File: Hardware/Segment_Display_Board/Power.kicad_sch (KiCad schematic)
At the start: 5 parts, among them J401 19V Input, U401 LM1117-5.0

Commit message: Fix stuff i guess goodnight"
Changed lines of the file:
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@@
     (title "Days Without Incident Sign")
     (date "2022-06-24")
-    (rev "v0.1-RC1")
+    (rev "${REVISION}")
     (company "FRC 1721")
+    (comment 4 "Release: ${FULL_REVISION}")
   )
   (junction (at 160.02 88.9) (diameter 0) (color 0 0 0 0)
@@
   )
   (junction (at 158.75 88.9) (diameter 0) (color 0 0 0 0)
+  )
+  (junction (at 134.62 88.9) (diameter 0) (color 0 0 0 0)
   )
   (wire (pts (xy 137.16 93.98) (xy 133.35 93.98))
@@
     (stroke (width 0) (type default) (color 0 0 0 0))
   )
-  (wire (pts (xy 133.35 88.9) (xy 137.16 88.9))
+  (wire (pts (xy 133.35 88.9) (xy 134.62 88.9))
     (stroke (width 0) (type default) (color 0 0 0 0))
   )
@@
   )
   (wire (pts (xy 167.64 88.9) (xy 170.18 88.9))
+    (stroke (width 0) (type default) (color 0 0 0 0))
+  )
+  (wire (pts (xy 134.62 88.9) (xy 137.16 88.9))
     (stroke (width 0) (type default) (color 0 0 0 0))
   )
@@
       (effects (font (size 1.27 1.27)) hide)
     )
+    (pin "1")
+  )
+  (symbol (lib_id "power:PWR_FLAG") (at 134.62 88.9 0) (unit 1)
+    (in_bom yes) (on_board yes) (fields_autoplaced)
+    (property "Reference" "#FLG0401" (id 0) (at 134.62 86.995 0)
+      (effects (font (size 1.27 1.27)) hide)
+    )
+    (property "Value" "PWR_FLAG" (id 1) (at 134.62 83.185 0)
+      (effects (font (size 1.27 1.27)) hide)
+    )
+    (property "Footprint" "" (id 2) (at 134.62 88.9 0)
+      (effects (font (size 1.27 1.27)) hide)
+    )
+    (property "Datasheet" "~" (id 3) (at 134.62 88.9 0)
+      (effects (font (size 1.27 1.27)) hide)
+    )

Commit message: Use a different regulator
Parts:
- U401: value LM1117-5.0 -> NCV1117ST50T3G
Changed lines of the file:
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@@
     (in_bom yes) (on_board yes)
     (property "Reference" "U401" (id 0) (at 151.13 95.25 0))
-    (property "Value" "LM1117-5.0" (id 1) (at 148.59 85.09 0))
+    (property "Value" "NCV1117ST50T3G" (id 1) (at 148.59 85.09 0))
     (property "Footprint" "Package_TO_SOT_SMD:SOT-223" (id 2) (at 148.59 88.9 0)
       (effects (font (size 1.27 1.27)) hide)

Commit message: include fixups fro EE
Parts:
- added C401: 10uf, Capacitor_SMD:CP_Elec_4x3, symbol Device:C_Polarized_Small
- added C402: 100nF, Capacitor_SMD:C_0805_2012Metric, symbol Device:C_Small
- added C404: 1uf, Capacitor_SMD:CP_Elec_4x3, symbol Device:C_Polarized_Small
- renumbered C401 to C403
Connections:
- net +19V: now also C401.1, C402.1
- net +5V: now also C404.1
- net GND: now also C401.2, C402.2, C404.2
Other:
- note removed: "I dont think this regulator can take this voltage, ask Mark."
- moved on the sheet: D401, J401, R401

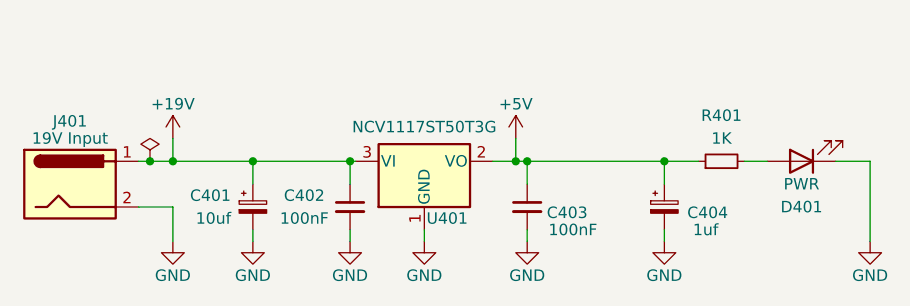
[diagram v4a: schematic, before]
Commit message: Change package for 1uF capacitor
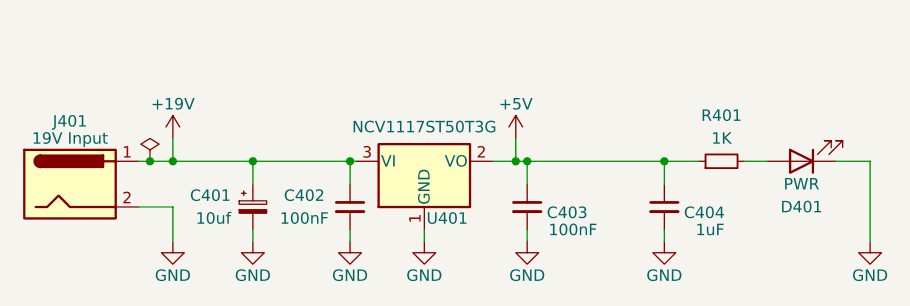
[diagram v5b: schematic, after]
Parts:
- removed C404: 1uf, Capacitor_SMD:CP_Elec_4x3, symbol Device:C_Polarized_Small
- added C404: 1uF, Capacitor_SMD:C_0805_2012Metric, symbol Device:C_Small
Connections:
- net +5V: now also C404.1
- net GND: now also C404.2
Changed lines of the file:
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@@
     (pin "1")
+  )
+  (symbol (lib_id "Device:C_Small") (at 175.26 93.98 0) (unit 1)
+    (in_bom yes) (on_board yes)
+    (property "Reference" "C404" (id 0) (at 179.705 94.615 0))
+    (property "Value" "1uF" (id 1) (at 180.34 96.52 0))
+    (property "Footprint" "Capacitor_SMD:C_0805_2012Metric" (id 2) (at 175.26 93.98 0)
+      (effects (font (size 1.27 1.27)) hide)
+    )
+    (property "Datasheet" "~" (id 3) (at 175.26 93.98 0)
+      (effects (font (size 1.27 1.27)) hide)
+    )
+    (pin "1")
+    (pin "2")
   )
   (symbol (lib_id "Device:C_Small") (at 160.02 93.98 0) (unit 1)
@@
       (effects (font (size 1.27 1.27)) hide)
     )
-    (pin "1")
-    (pin "2")
-  )
-  (symbol (lib_id "Device:C_Polarized_Small") (at 175.26 93.98 0) (unit 1)
-    (in_bom yes) (on_board yes)
-    (property "Reference" "C404" (id 0) (at 177.8 94.615 0)
-      (effects (font (size 1.27 1.27)) (justify left))
-    )
-    (property "Value" "1uf" (id 1) (at 178.435 96.52 0)
-      (effects (font (size 1.27 1.27)) (justify left))
-    )
-    (property "Footprint" "Capacitor_SMD:CP_Elec_4x3" (id 2) (at 175.26 93.98 0)
-      (effects (font (size 1.27 1.27)) hide)
-    )
-    (property "Datasheet" "~" (id 3) (at 175.26 93.98 0)
-      (effects (font (size 1.27 1.27)) hide)
-    )
